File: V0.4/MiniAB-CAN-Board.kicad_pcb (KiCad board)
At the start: 4 copper layers, 51 x 45 mm, 133 parts, among them J1 PC-FAN, J10 USB_B_Micro, J11 CAN, J12 ENDSTOP1, J13 ENDSTOP2, J14 PROBE, J2 PC-FAN, J3 HE-FAN, J4 TH0, J5 I2C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

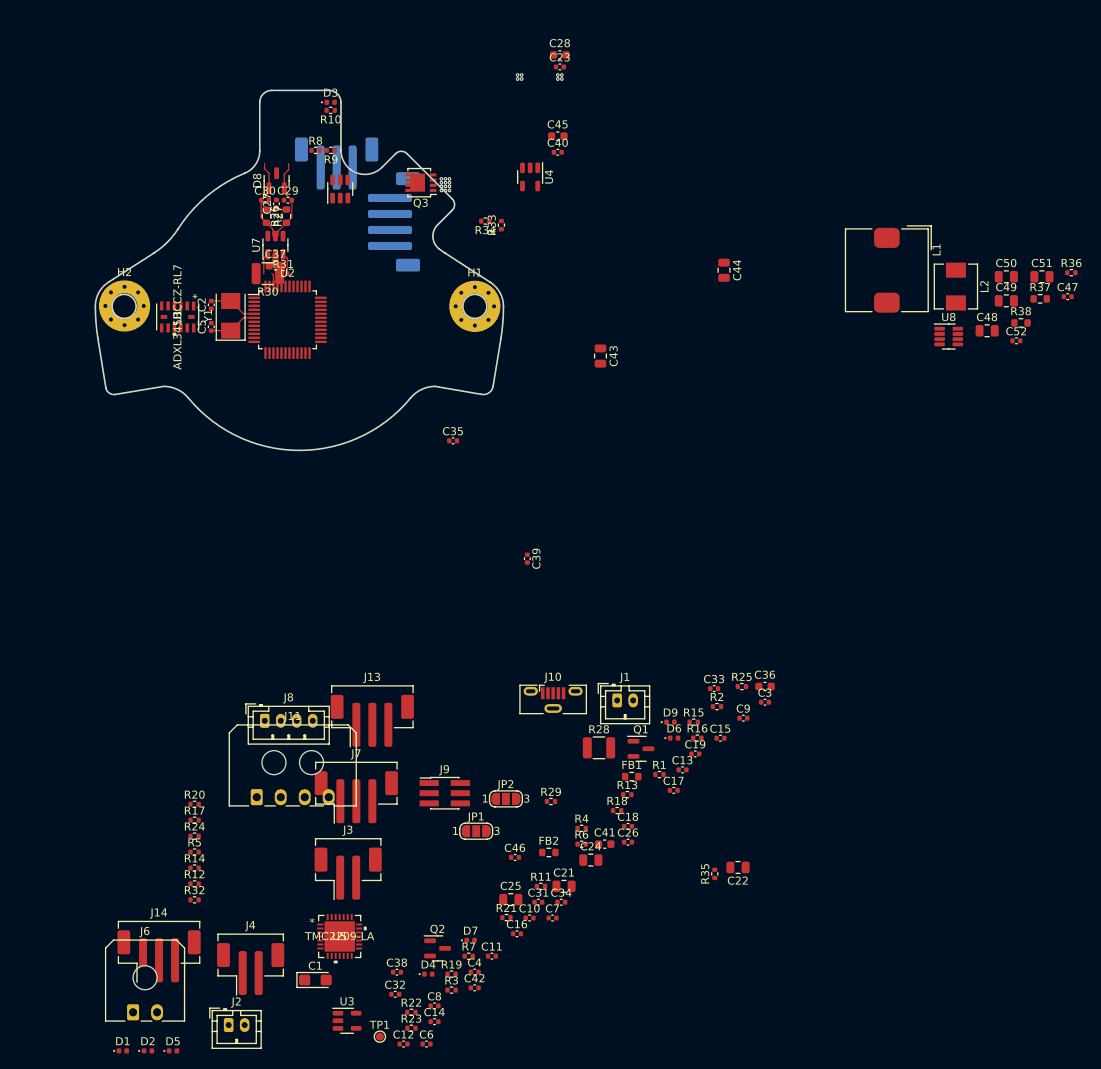
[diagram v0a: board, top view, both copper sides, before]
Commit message: Add THT JST version with new DCDC converter
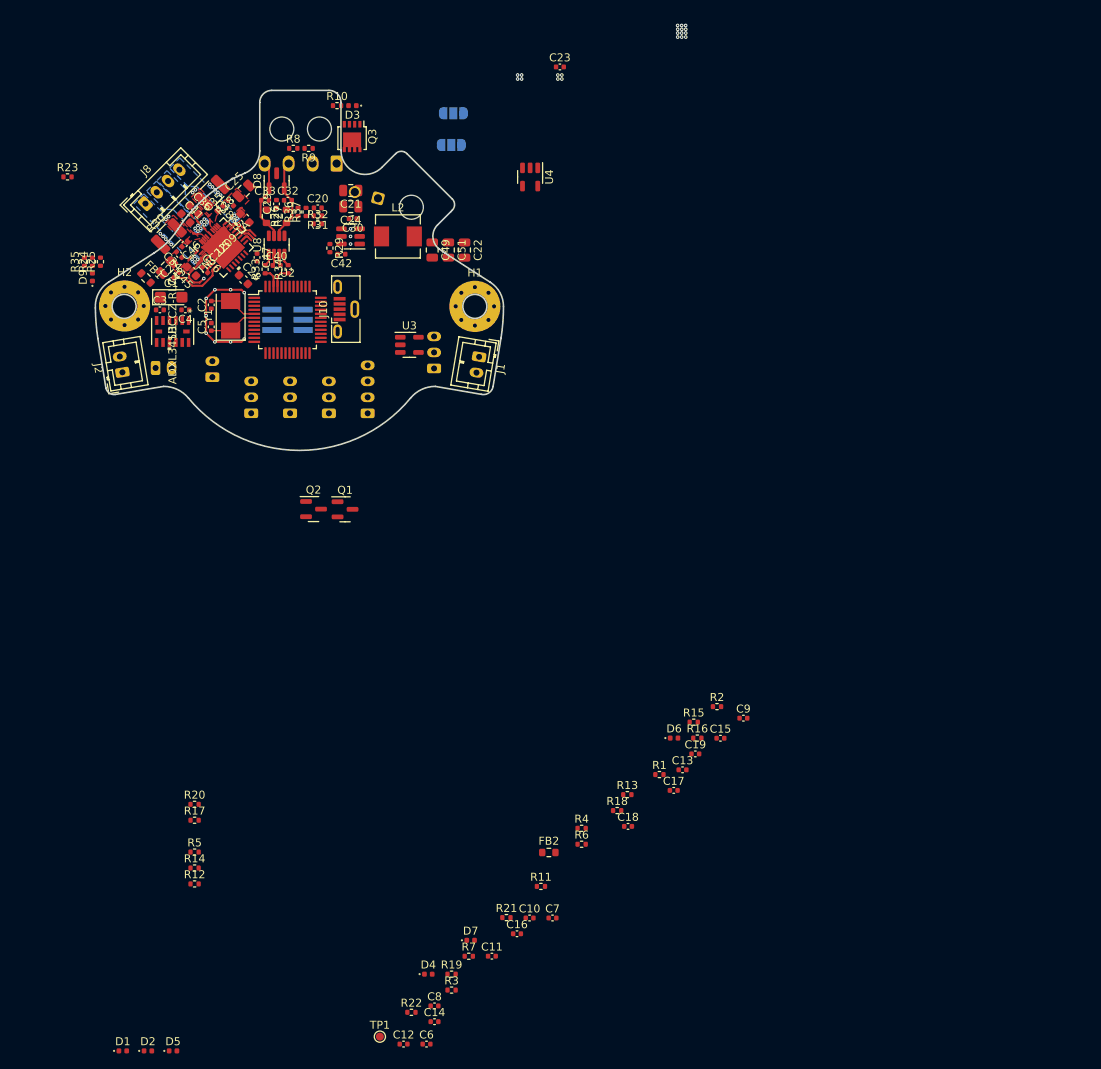
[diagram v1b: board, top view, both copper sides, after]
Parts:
- removed C31: 100n/35V, Capacitor_SMD:C_0402_1005Metric
- removed C39: 100n, Capacitor_SMD:C_0402_1005Metric
- removed C44, C48, C50: 22u, Capacitor_SMD:C_0805_2012Metric
- removed C52: 75p, Capacitor_SMD:C_0402_1005Metric
- removed L1: 15u, Inductor_SMD:L_TDK_SLF10145
- removed R38: 13k, Resistor_SMD:R_0603_1608Metric
- removed U7: TPS54202DDC, Package_TO_SOT_SMD:SOT-23-6
- added C20: 10p, Capacitor_SMD:C_0402_1005Metric, F.Cu at (216.1, 59.5)
- C22: value 10u/35V -> 22u
- C25: value 10u/35V -> 100u/35V, Low ESR
- J11, J9, JP1, JP2: moved to B.Cu
- J12: footprint Connector_JST:JST_PH_B3B-PH-SM4-TB_1x03-1MP_P2.00mm_Vertical -> Connector_JST:JST_PH_B3B-PH-K_1x03_P2.00mm_Vertical
- J13, J14, J7: footprint Connector_JST:JST_PH_B3B-PH-SM4-TB_1x03-1MP_P2.00mm_Vertical -> Connector_JST:JST_PH_B3B-PH-K_1x03_P2.00mm_Vertical; moved to B.Cu
- J3, J4: footprint Connector_JST:JST_PH_B2B-PH-SM4-TB_1x02-1MP_P2.00mm_Vertical -> Connector_JST:JST_PH_B2B-PH-K_1x02_P2.00mm_Vertical; moved to B.Cu
- J5: footprint Connector_JST:JST_PH_B4B-PH-SM4-TB_1x04-1MP_P2.00mm_Vertical -> Connector_JST:JST_PH_B4B-PH-K_1x04_P2.00mm_Vertical
- J6: footprint Connector_Molex:Molex_Micro-Fit_3.0_43650-0200_1x02_P3.00mm_Horizontal -> Connector_Molex:Molex_Micro-Fit_3.0_43045-0200_2x01_P3.00mm_Horizontal; moved to B.Cu
- R37: value 100k -> 0; footprint Resistor_SMD:R_0603_1608Metric -> Resistor_SMD:R_0402_1005Metric
- moved R23 114.8 mm to (184.9, 55.6)
- moved R35 109.8 mm to (187.0, 66.2)
- moved J6 106.3 mm to (223.7, 58.3), turned to 75 degrees
- moved C47 101.4 mm to (208.6, 65.7), turned to -90 degrees
- moved C32 100.2 mm to (212.4, 58.6)
- moved C38 98.4 mm to (205.3, 58.9), turned to 135 degrees
- moved R36 97.0 mm to (213.7, 60.0), turned to 90 degrees
- moved R25 96.2 mm to (189.0, 66.2), turned to 90 degrees
- moved C25 94.7 mm to (206.9, 57.4), turned to 45 degrees
- moved C41 94.2 mm to (199.6, 60.8), turned to -45 degrees
- moved C34 94.0 mm to (198.8, 65.4), turned to 135 degrees
- moved C42 93.2 mm to (219.1, 65.3), turned to 180 degrees
- moved C36 93.0 mm to (200.7, 59.7), turned to -45 degrees
- moved R37 92.4 mm to (214.7, 60.0), turned to 90 degrees
- moved D9 91.2 mm to (188.0, 68.2), turned to 90 degrees
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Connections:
- net Net-(R29-Pad1) renamed /BOOT
- C22 pad 1: TMC_VS -> +5V
- C42 pad 1: Net-(C42-Pad1) -> /SW
- C49 pad 1: Net-(C49-Pad1) -> +5V
- C51 pad 1: Net-(C49-Pad1) -> +5V
- L2 pad 1: Net-(C42-Pad2) -> /SW
- L2 pad 2: Net-(C49-Pad1) -> +5V
- R29 pad 2: Net-(C42-Pad1) -> Net-(C42-Pad2)
- R31 pad 1: Net-(R31-Pad1) -> /FB
- R31 pad 2: Net-(C49-Pad1) -> Net-(R31-Pad2)
- R32 pad 2: Net-(R31-Pad1) -> /FB
- R36 pad 1: +5V -> Net-(R31-Pad2)
- R36 pad 2: Net-(C52-Pad1) -> +5V
- R37 pad 1: Net-(C52-Pad1) -> Net-(R31-Pad2)
- R37 pad 2: /FB -> Net-(C20-Pad1)
- U6 pad 2: Net-(C42-Pad2) -> /SW
- U6 pad 4: Net-(R31-Pad1) -> /FB
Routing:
- net GND: track 7.31 -> 19.0 mm, vias 12 -> 38
- net CANH: track 0.00 -> 10.4 mm
- net CANL: track 20.7 -> 10.4 mm
- net Net-(C27-Pad1): track 0.00 -> 7.07 mm
- net ST_ENN: track 0.00 -> 5.85 mm, vias 0 -> 1
- net Net-(R35-Pad1): track 0.00 -> 3.73 mm
- net ST_DIR: track 0.00 -> 3.07 mm
- net CAN_RX: track 0.00 -> 2.75 mm
- net Net-(C29-Pad1): track 2.71 -> 0.00 mm
- net TMC_VS: track 2.63 -> 0.00 mm
- net Net-(R34-Pad2): track 0.00 -> 1.59 mm
- net Net-(R33-Pad2): track 0.00 -> 1.59 mm
- net VBAT: track 0.00 -> 1.50 mm
- net ST_STEP: track 0.00 -> 1.41 mm
- net Net-(C26-Pad2): track 0.00 -> 1.34 mm
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- added copper zone on B.Cu, net A1
- added copper zone on F.Cu, net A1
- added copper zone on B.Cu, net A2
- added copper zone on F.Cu, net A2
- added copper zone on B.Cu, net B1
- added copper zone on F.Cu, net B1
- added copper zone on B.Cu, net B2
- added copper zone on F.Cu, net B2
- added copper zone on F.Cu, net BRA
- added copper zone on F.Cu, net BRB
- added copper zone on F.Cu, net TMC_VS

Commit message: Update PCB
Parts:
- J10, TP1: moved to B.Cu
- moved C6 98.4 mm to (206.7, 68.4), turned to 90 degrees
- moved TP1 96.4 mm to (213.6, 67.3), turned to 180 degrees
- moved C12 91.9 mm to (206.7, 74.4), turned to 90 degrees
- moved C8 90.5 mm to (217.1, 69.8)
- moved C11 89.9 mm to (207.7, 68.4), turned to 90 degrees
- moved C16 83.1 mm to (244.4, 67.3), turned to -90 degrees
- moved C9 81.8 mm to (208.7, 68.4), turned to 90 degrees
- moved R4 78.4 mm to (213.6, 67.2), turned to -90 degrees
- moved C7 76.3 mm to (211.4, 80.1), turned to 90 degrees
- moved C13 75.8 mm to (207.2, 77.2)
- moved C10 75.2 mm to (216.5, 77.8)
- moved FB2 72.2 mm to (207.5, 78.4)
- moved C18 68.5 mm to (244.4, 69.1), turned to 90 degrees
- moved C15 64.3 mm to (239.9, 67.3), turned to -90 degrees
- moved R11 45.6 mm to (213.7, 110.3)
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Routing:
- net Net-(J1-Pad2): track 0.00 -> 54.9 mm
- net Net-(D1-Pad1): track 0.00 -> 51.2 mm
- net SCLK: track 0.00 -> 26.0 mm
- net ST_STEP: track 1.41 -> 22.9 mm, vias 0 -> 2
- net ST_DIR: track 3.07 -> 23.9 mm, vias 0 -> 2
- net ST_RX: track 0.00 -> 20.6 mm, vias 0 -> 2
- net ADXL_CS: track 0.00 -> 20.5 mm
- net TMC_VS: track 0.00 -> 19.4 mm, vias 0 -> 8
- net ST_TX: track 0.00 -> 18.1 mm, vias 0 -> 2
- net ADXL_INT1: track 0.00 -> 17.2 mm
- net SDO: track 0.00 -> 16.7 mm
- net SDI: track 0.00 -> 16.1 mm
- net ST_DIAG: track 0.00 -> 16.0 mm, vias 0 -> 2
- net NEOPIXEL: track 0.00 -> 15.9 mm
- net VBAT: track 1.50 -> 16.7 mm, vias 0 -> 8
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- added copper zone on F.Cu, net +5V
- added copper zone on B.Cu, net /SW
- added copper zone on F.Cu, net /SW
- added copper zone on B.Cu, net GND
- added copper zone on F.Cu, net GND
- added copper zone on In2.Cu, net GND
- added copper zone on B.Cu, net TMC_VS
- added copper zone on In1.Cu, net VBAT
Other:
- board size 51 x 45 mm -> 51.2 x 45 mm

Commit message: Update DCDC Section
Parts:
- R23: value 10k -> 100k
- moved C23 68.5 mm to (216.5, 103.5)
- moved C18 22.0 mm to (222.5, 72.1)
- moved R36 21.6 mm to (235.1, 63.2)
- moved R37 21.6 mm to (236.1, 63.2)
- moved C16 20.0 mm to (225.4, 73.5), turned to 180 degrees
- moved U4 17.5 mm to (225.1, 71.3), turned to 180 degrees
- moved Q3 15.5 mm to (220.4, 50.5), turned to -90 degrees
- moved C15 14.7 mm to (225.4, 69.1), turned to 180 degrees
- moved Q1 12.6 mm to (229.7, 89.7), turned to 90 degrees
- moved C22 6.48 mm to (225.1, 75.0), turned to 180 degrees
- moved L2 3.56 mm to (222.9, 61.7)
- moved R29 3.49 mm to (214.4, 63.3)
- moved U6 3.49 mm to (217.0, 61.9)
- moved C42 3.49 mm to (215.8, 64.1)
- moved C21 3.48 mm to (217.0, 56.1)
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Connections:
- U2 pad 19: ST_ENN -> unconnected-(U2-Pad19)
- U2 pad 2: unconnected-(U2-Pad2) -> ST_ENN
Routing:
- net ST_ENN: track 4.76 -> 15.7 mm, vias 1 -> 3
- net VBAT: track 16.7 -> 22.2 mm, vias 8 -> 17
- net /FB: track 4.92 -> 0.00 mm
- net +5V: track 9.80 -> 5.22 mm
- net Net-(J7-Pad2): track 2.78 -> 0.00 mm
- net BOOT1: track 12.5 -> 10.1 mm
- net OSC_OUT: track 4.92 -> 7.34 mm
- net OSC_IN: track 4.62 -> 7.04 mm
- net Net-(R31-Pad2): track 2.40 -> 0.00 mm
- net NEOPIXEL: track 15.9 -> 17.4 mm
- net GND: track 18.9 -> 20.2 mm, vias 145 -> 131
- net unconnected-(U2-Pad19): track 0.00 -> 1.23 mm
- net USB_DP: track 7.16 -> 6.07 mm
- net Net-(C20-Pad1): track 0.98 -> 0.00 mm
- net USB_DM: track 6.97 -> 6.01 mm
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
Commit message: V0.4 finished
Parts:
- added TP2: 3V3, TestPoint:TestPoint_Pad_D1.0mm, B.Cu at (210.3, 66.3)
- added TP3: 24V, TestPoint:TestPoint_Pad_D1.0mm, B.Cu at (209.1, 57.7)
- added TP4: GND, TestPoint:TestPoint_Pad_D1.0mm, B.Cu at (196.6, 70.3)
- J1, J2: value PC-FAN -> PCF
- J3: value HE-FAN -> HEF
- J9: value Conn_02x03_Top_Bottom -> DEBUG
- moved D4 70.6 mm to (217.9, 46.2), turned to 30 degrees
- moved D7 68.3 mm to (211.9, 47.3), turned to 150 degrees
- moved D6 66.1 mm to (210.0, 46.2), turned to 150 degrees
- moved R13 66.0 mm to (214.0, 47.8), turned to 180 degrees
- moved D5 60.6 mm to (229.6, 73.5), turned to 180 degrees
- moved D1 56.6 mm to (222.1, 77.4), turned to -90 degrees
- moved R17 51.2 mm to (207.9, 45.8), turned to 180 degrees
- moved R20 47.6 mm to (209.9, 47.7), turned to 180 degrees
- moved C14 45.7 mm to (212.4, 79.8), turned to -90 degrees
- moved R7 44.7 mm to (203.6, 81.8), turned to -90 degrees
- moved D2 44.2 mm to (202.6, 81.8), turned to 90 degrees
- moved C17 43.3 mm to (219.0, 74.8)
- moved R22 41.7 mm to (211.4, 82.2), turned to -90 degrees
- moved R1 40.9 mm to (220.5, 75.3), turned to -90 degrees
- moved R3 39.8 mm to (222.1, 79.4), turned to 90 degrees
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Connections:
- J12 pad 1: +5V -> VBAT
- J13 pad 1: +5V -> VBAT
- J14 pad 1: +5V -> VBAT
- U2 pad 10: LED0 -> unconnected-(U2-Pad10)
- U2 pad 11: unconnected-(U2-Pad11) -> LED0
- U2 pad 12: TH0 -> unconnected-(U2-Pad12)
- U2 pad 18: NEOPIXEL -> HE-FAN
- U2 pad 19: unconnected-(U2-Pad19) -> TH0
- U2 pad 26: HE-FAN -> ENDSTOP2
- U2 pad 27: HEATER -> unconnected-(U2-Pad27)
- U2 pad 28: ST_STEP -> ENDSTOP1
- U2 pad 29: ST_DIR -> unconnected-(U2-Pad29)
- U2 pad 30: ST_TX -> PROBE
- U2 pad 31: ST_RX -> NEOPIXEL
- U2 pad 39: PROBE -> ST_DIR
- U2 pad 40: ENDSTOP1 -> ST_STEP
- U2 pad 41: ENDSTOP2 -> HEATER
- U2 pad 42: unconnected-(U2-Pad42) -> ST_TX
- U2 pad 43: unconnected-(U2-Pad43) -> ST_RX
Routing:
- net LED0: track 0.00 -> 55.2 mm, vias 0 -> 2
- net Net-(J3-Pad2): track 0.00 -> 39.3 mm
- net HEATER: track 0.00 -> 31.9 mm, vias 0 -> 2
- net Net-(J1-Pad2): track 54.9 -> 84.8 mm, vias 0 -> 2
- net TMC_VS: track 19.4 -> 47.9 mm
- net +5V: track 5.22 -> 33.3 mm, vias 0 -> 6
- net Net-(J4-Pad1): track 0.00 -> 19.9 mm, vias 0 -> 1
- net PROBE: track 0.00 -> 17.5 mm, vias 0 -> 2
- net GND: track 20.2 -> 34.3 mm, vias 131 -> 209
- net ENDSTOP1: track 0.00 -> 13.4 mm, vias 0 -> 2
- net Net-(D1-Pad1): track 51.2 -> 63.0 mm
- net ENDSTOP2: track 0.00 -> 11.0 mm, vias 0 -> 2
- net ST_STEP: track 22.9 -> 12.7 mm, vias 2 -> 0
- net ST_RX: track 20.6 -> 10.7 mm
- net ST_TX: track 18.1 -> 8.65 mm
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- added copper zone on F.Cu, net Net-(D3-Pad1)
- added copper zone on F.Cu, net VBAT
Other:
- board size 51.2 x 45 mm -> 51.1 x 45.2 mm

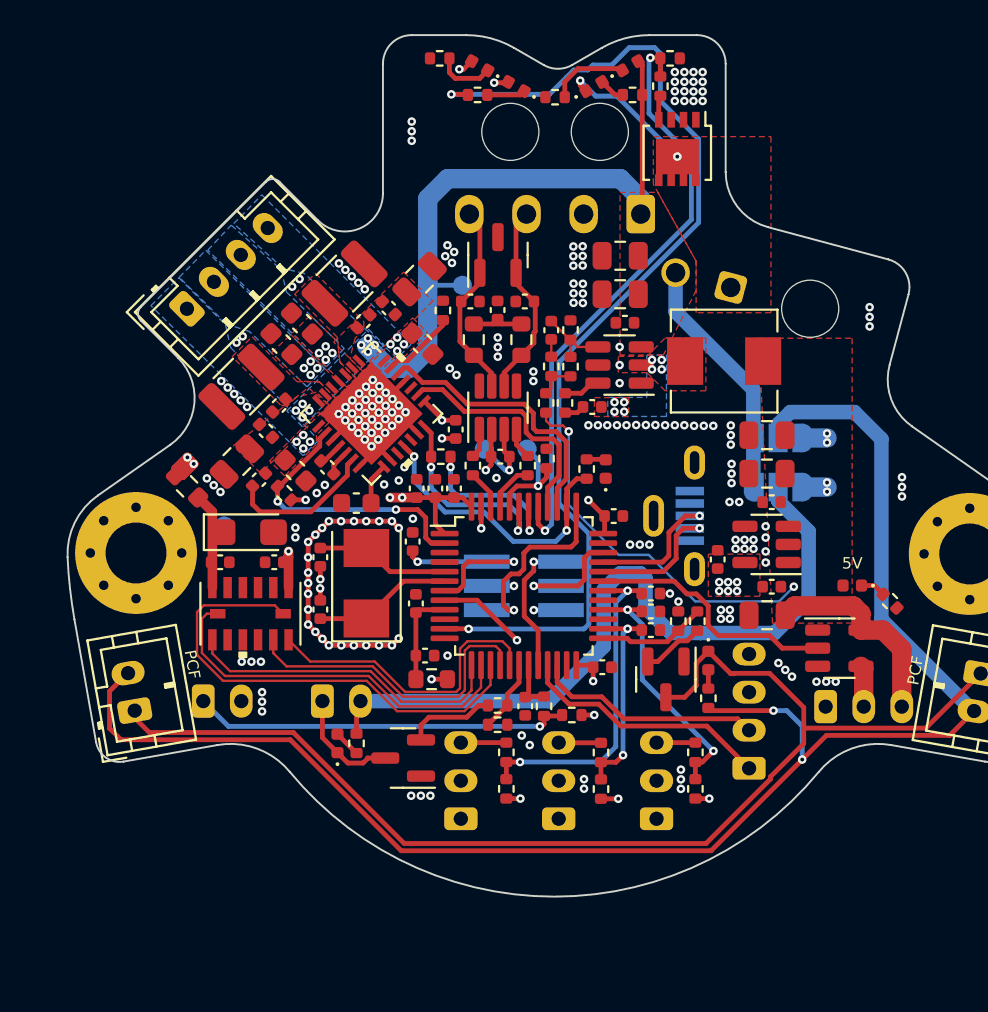
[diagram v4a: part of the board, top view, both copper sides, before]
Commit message: Fix GND connection on TCAN330
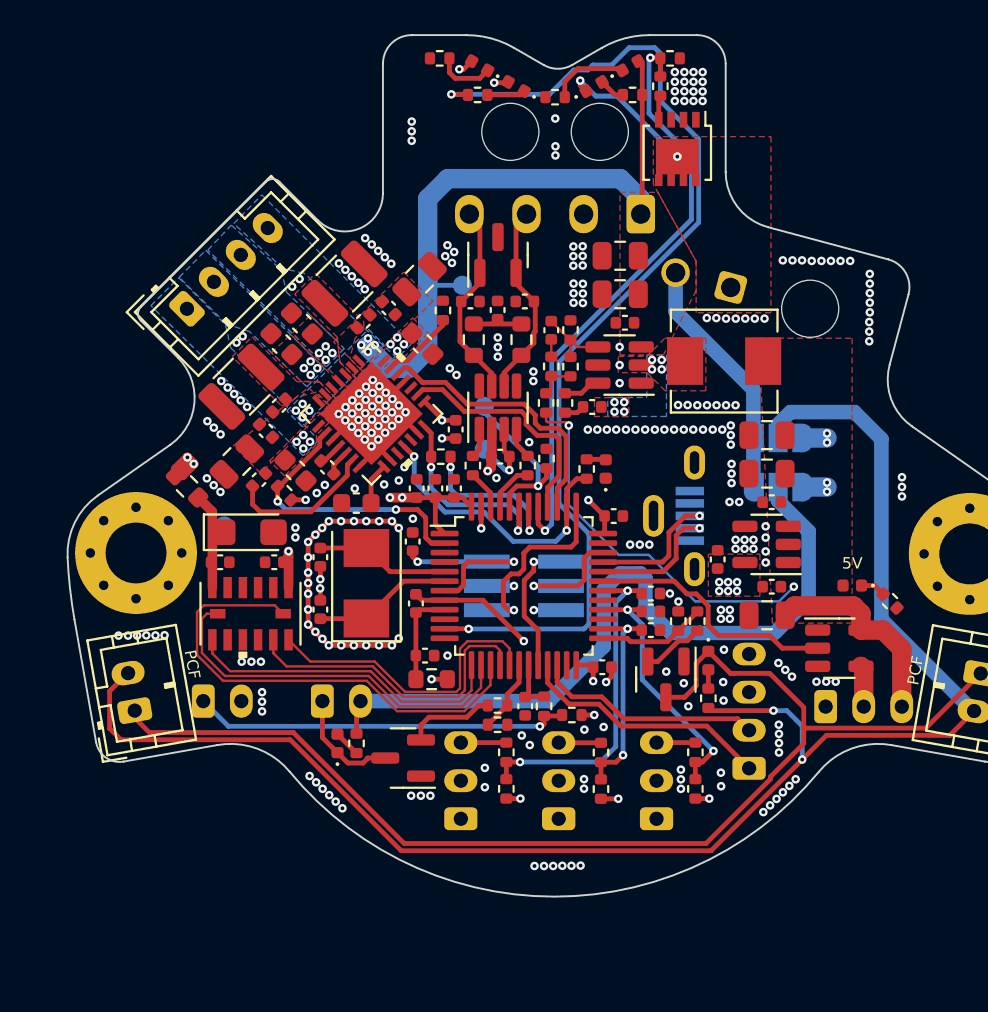
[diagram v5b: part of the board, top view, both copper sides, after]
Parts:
- moved TP1 3.17 mm to (210.3, 64.1)
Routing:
- net Net-(R4-Pad2): track 5.65 -> 8.82 mm
- net GND: track 34.3 -> 37.2 mm, vias 209 -> 291

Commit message: Add silkscreen annotations
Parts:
- moved R11 0.18 mm to (214.9, 80.1)
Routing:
- net GND: vias 291 -> 287
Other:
- board text added: "24V"
- board text added: "3V3"
- board text added: "5V"
- board text added: "A1"
- board text added: "A2"
- board text added: "B1"
- board text added: "B2"
- board text added: "BOOT1"
- board text added: "CANH"
- board text added: "CANL"
- board text added: "GND"
- board text added: "NRST"
- board text added: "PA10"
- board text added: "PA9"
- board text added: "PB0"
- board text added: "PB1"
- board text added: "PB12"
- board text added: "PB13"
- board text added: "PB15"
- board text added: "SCL"
- board text added: "SDA"
- board text added: "SWCLK"
- board text added: "SWDIO"
- board text added: "V+"
